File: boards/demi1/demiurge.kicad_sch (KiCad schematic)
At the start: 140 parts, among them J12 Micro_SD_Card_Det_Hirose_DM3AT, J2 Conn_01x06, U1 MCP6002, U10 TL072, U11 TL072, U13 CH32V307RCT6, U2 AMS1117-3.3, U3 MCP6002, U4 AW20036, U5 W25Q128JVS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

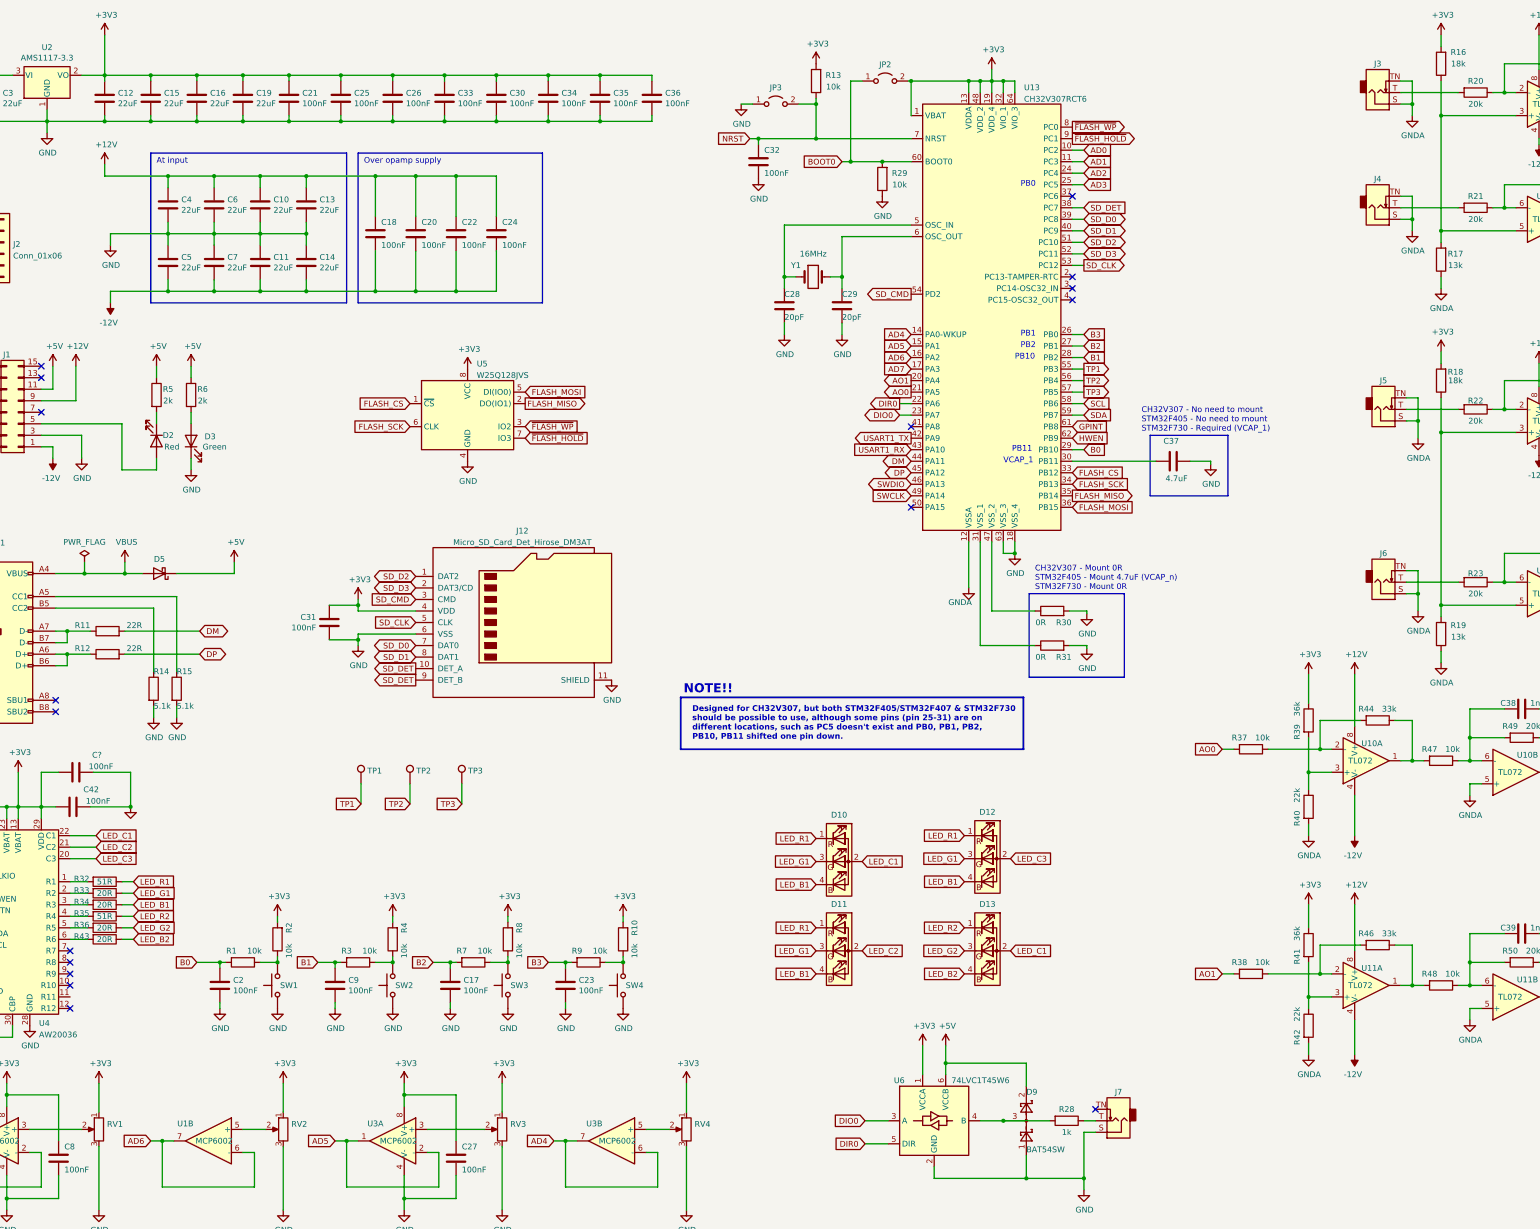
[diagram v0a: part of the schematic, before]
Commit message: Adding testpad for MCO pin, for instance to check clock speeds.
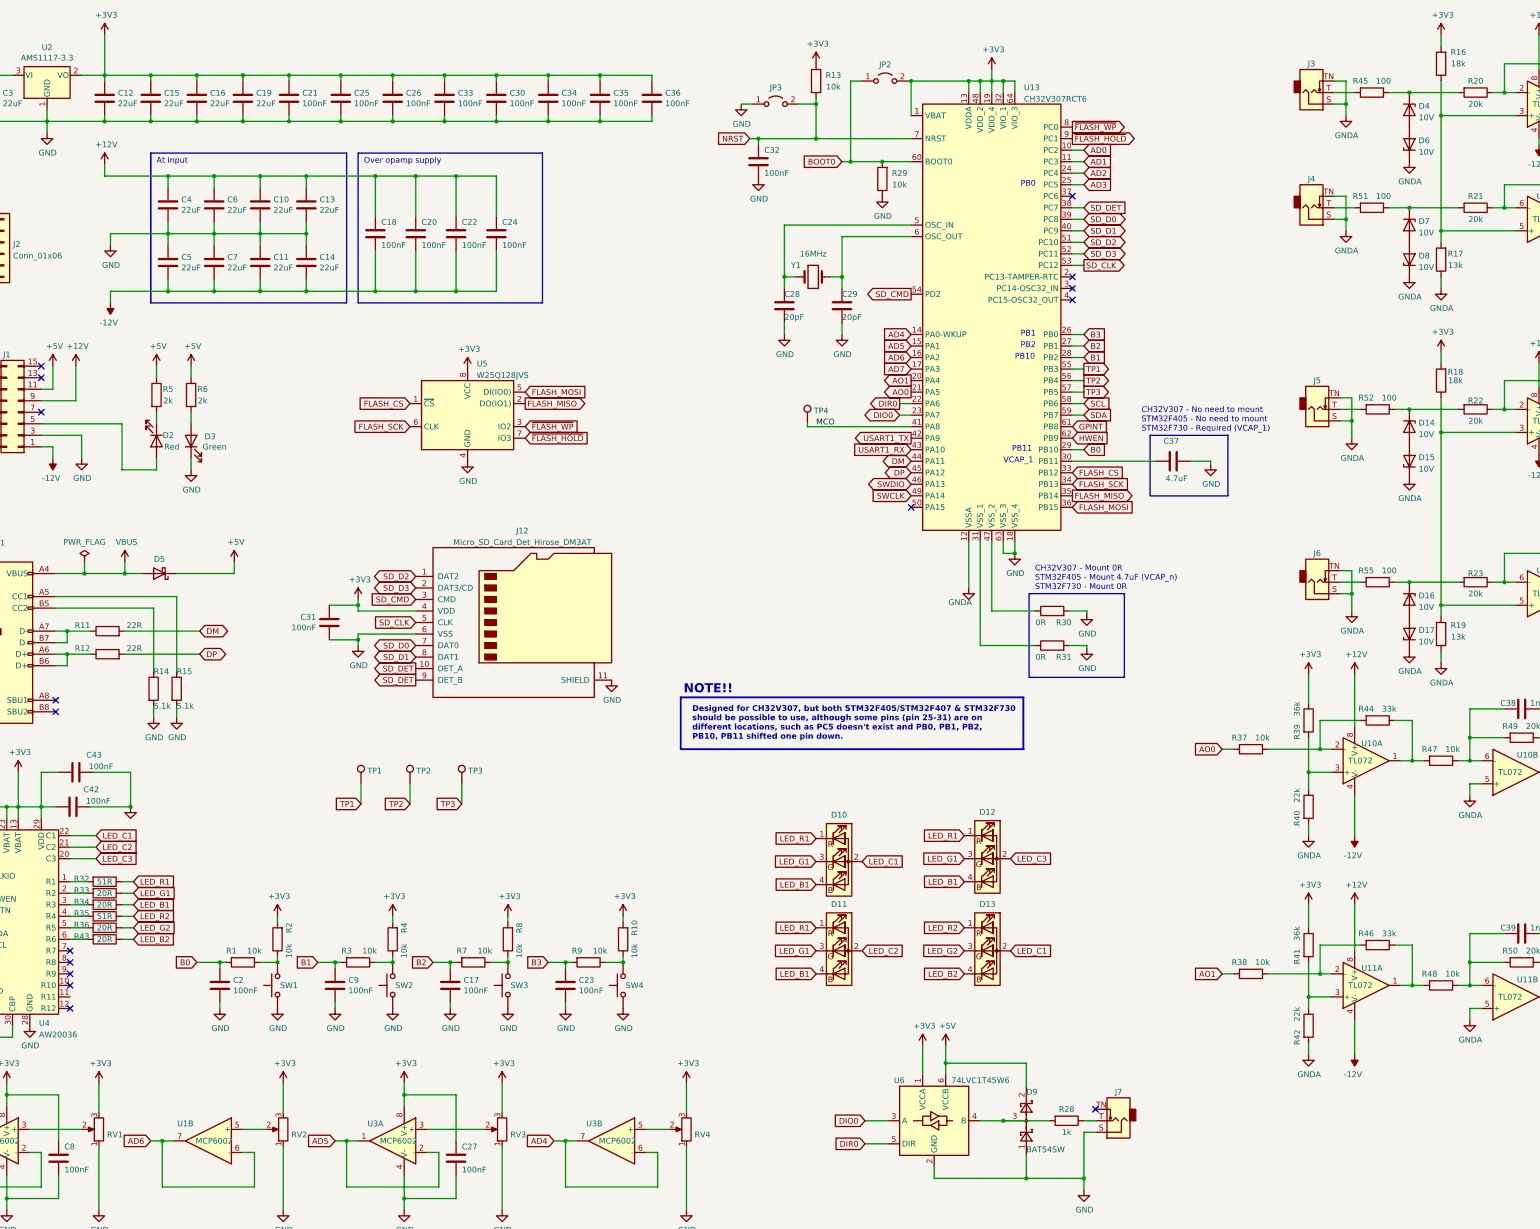
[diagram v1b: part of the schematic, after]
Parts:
- added D14, D15, D16, D17, D4, D6, D7, D8: 10V, Diode_SMD:D_SOD-323, symbol Device:D_Zener
- added R45, R51, R52, R55: 100, Resistor_SMD:R_0603_1608Metric, symbol Device:R
- added TP4: SWO, TestPoint:TestPoint_Pad_1.5x1.5mm, symbol Connector:TestPoint
- JP2, JP3: footprint Jumper:SolderJumper-2_P1.3mm_Open_RoundedPad1.0x1.5mm -> Capacitor_SMD:C_1206_3216Metric
- gave numbers to parts that had none: 1
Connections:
- net +3V3: now also RV1.3, RV2.3, RV3.3, RV4.3; no longer RV1.1, RV2.1, RV3.1, RV4.1
- net GND: now also RV1.1, RV2.1, RV3.1, RV4.1; no longer RV1.3, RV2.3, RV3.3, RV4.3
- net GNDA: now also D15.1 (K), D17.1 (K), D6.1 (K), D8.1 (K)
- net at J4.T: now also R51.2; no longer R21.2
- net at J3.T: now also R45.2; no longer R20.2
- net at J5.T: now also R52.2; no longer R22.2
- net at J6.T: now also R55.2; no longer R23.2
- net MCO: now reaches U13.41 (PA8)
- net MCO: now also TP4.1
- new net: D4.1 (K), R20.2, R45.1
- new net: D7.1 (K), R21.2, R51.1
- new net: D14.1 (K), R22.2, R52.1
- new net: D16.1 (K), R23.2, R55.1
- new net: D7.2 (A), D8.2 (A)
- new net: D14.2 (A), D15.2 (A)
- new net: D4.2 (A), D6.2 (A)
- new net: D16.2 (A), D17.2 (A)
- no-connect marks 23 -> 22
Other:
- moved on the sheet: J3, J4, J5, J6, RV1, RV2, RV3, RV4

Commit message: RevF order made at jlcpcb.
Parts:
- C40: LCSC C14663 -> C15849
- J2: LCSC (none) -> C37208
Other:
- title: Demiurge -> AAA Demiurge 1
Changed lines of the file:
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@@
   (paper "A3")
   (title_block
-    (title "Demiurge")
+    (title "AAA Demiurge 1")
+    (date "2022-08-11")
     (rev "F")
     (company "Awesome Audio Apparatus")
@@
       (effects (font (size 1.27 1.27)) hide)
     )
+    (property "LCSC" "C37208" (id 4) (at 34.925 64.77 0)
+      (effects (font (size 1.27 1.27)) hide)
+    )
     (pin "1")
     (pin "2")
@@
   (symbol (lib_id "Device:C") (at 27.305 240.03 90) (unit 1)
     (in_bom yes) (on_board yes)
-    (property "Reference" "C40" (id 0) (at 31.115 238.76 90)
+    (property "Reference" "C40" (id 0) (at 32.385 238.76 90)
       (effects (font (size 1.27 1.27)) (justify left))
     )
@@
       (effects (font (size 1.27 1.27)) hide)
     )
-    (property "LCSC" "C14663" (id 4) (at 27.305 240.03 0)
+    (property "LCSC" "C15849" (id 4) (at 27.305 240.03 0)
       (effects (font (size 1.27 1.27)) hide)
     )

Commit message: Forgot I2C resistors. Grrr...
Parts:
- added R56, R57: 3k3, Resistor_SMD:R_0603_1608Metric, symbol Device:R
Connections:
- net +3V3: now also R56.2, R57.2
- net SCL: now also R56.1
- net SDA: now also R57.1
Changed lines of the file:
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@@
   (title_block
     (title "AAA Demiurge 1")
-    (date "2022-08-11")
-    (rev "F")
+    (rev "G")
     (company "Awesome Audio Apparatus")
   )
@@
   (junction (at 365.76 139.7) (diameter 0) (color 0 0 0 0)
   )
+  (junction (at 24.765 217.17) (diameter 0) (color 0 0 0 0)
+  )
   (junction (at 330.835 59.69) (diameter 0) (color 0 0 0 0)
   )
@@
   (junction (at 166.37 38.1) (diameter 0) (color 0 0 0 0)
   )
+  (junction (at 19.685 231.14) (diameter 0) (color 0 0 0 0)
+  )
   (junction (at 257.81 133.35) (diameter 0) (color 0 0 0 0)
   )
@@
   (junction (at 113.03 144.78) (diameter 0) (color 0 0 0 0)
   )
+  (junction (at 19.685 219.71) (diameter 0) (color 0 0 0 0)
+  )
   (junction (at 71.12 50.165) (diameter 0) (color 0 0 0 0)
   )
@@
     (stroke (width 0) (type default) (color 0 0 0 0))
   )
+  (wire (pts (xy 17.78 219.71) (xy 19.685 219.71))
+    (stroke (width 0) (type default) (color 0 0 0 0))
+  )
   (wire (pts (xy 250.19 29.21) (xy 250.19 31.75))
     (stroke (width 0) (type default) (color 0 0 0 0))
@@
     (stroke (width 0) (type default) (color 0 0 0 0))
   )
+  (wire (pts (xy 13.97 227.33) (xy 13.97 231.14))
+    (stroke (width 0) (type default) (color 0 0 0 0))
+  )
   (wire (pts (xy 45.72 97.155) (xy 45.72 92.075))
     (stroke (width 0) (type default) (color 0 0 0 0))
@@
     (stroke (width 0) (type default) (color 0 0 0 0))
   )
+  (wire (pts (xy 13.97 231.14) (xy 19.685 231.14))
+    (stroke (width 0) (type default) (color 0 0 0 0))
+  )
   (wire (pts (xy 48.895 150.495) (xy 53.975 150.495))
     (stroke (width 0) (type default) (color 0 0 0 0))
@@
     (stroke (width 0) (type default) (color 0 0 0 0))
   )
+  (wire (pts (xy 17.78 217.17) (xy 24.765 217.17))
+    (stroke (width 0) (type default) (color 0 0 0 0))
+  )
   (wire (pts (xy 273.05 57.15) (xy 270.51 57.15))
     (stroke (width 0) (type default) (color 0 0 0 0))
@@
     (stroke (width 0) (type default) (color 0 0 0 0))
   )
+  (wire (pts (xy 24.765 217.17) (xy 24.765 220.98))
+    (stroke (width 0) (type default) (color 0 0 0 0))
+  )
   (wire (pts (xy 234.95 29.21) (xy 247.65 29.21))
     (stroke (width 0) (type default) (color 0 0 0 0))
@@
     (stroke (width 0) (type default) (color 0 0 0 0))
   )
+  (wire (pts (xy 19.685 220.98) (xy 19.685 219.71))
+    (stroke (width 0) (type default) (color 0 0 0 0))
+  )
   (wire (pts (xy 113.03 152.4) (xy 113.03 153.67))
     (stroke (width 0) (type default) (color 0 0 0 0))
@@
     (stroke (width 0) (type default) (color 0 0 0 0))
   )
+  (wire (pts (xy 19.685 219.71) (xy 29.21 219.71))
+    (stroke (width 0) (type default) (color 0 0 0 0))
+  )
   (wire (pts (xy 270.51 67.31) (xy 273.05 67.31))
     (stroke (width 0) (type default) (color 0 0 0 0))
@@
     (stroke (width 0) (type default) (color 0 0 0 0))
   )
+  (wire (pts (xy 24.765 231.14) (xy 24.765 228.6))
+    (stroke (width 0) (type default) (color 0 0 0 0))
+  )
+  (wire (pts (xy 19.685 231.14) (xy 24.765 231.14))
+    (stroke (width 0) (type default) (color 0 0 0 0))
+  )
   (wire (pts (xy 35.56 191.77) (xy 35.56 189.23))
     (stroke (width 0) (type default) (color 0 0 0 0))
@@
     (stroke (width 0) (type default) (color 0 0 0 0))
   )
+  (wire (pts (xy 19.685 228.6) (xy 19.685 231.14))
+    (stroke (width 0) (type default) (color 0 0 0 0))
+  )
   (wire (pts (xy 351.79 106.68) (xy 351.79 99.06))
     (stroke (width 0) (type default) (color 0 0 0 0))
@@
     (stroke (width 0) (type default) (color 0 0 0 0))
   )
+  (wire (pts (xy 24.765 217.17) (xy 29.21 217.17))
+    (stroke (width 0) (type default) (color 0 0 0 0))
+  )
   (wire (pts (xy 234.95 60.96) (xy 207.01 60.96))
     (stroke (width 0) (type default) (color 0 0 0 0))
@@
     )
   )
-  (global_label "SDA" (shape input) (at 29.21 217.17 180) (fields_autoplaced)
+  (global_label "SDA" (shape input) (at 17.78 217.17 180) (fields_autoplaced)
     (effects (font (size 1.27 1.27)) (justify right))
-    (property "Intersheet References" "${INTERSHEET_REFS}" (id 0) (at 7.62 5.08 0)
+    (property "Intersheet References" "${INTERSHEET_REFS}" (id 0) (at -3.81 5.08 0)
       (effects (font (size 1.27 1.27)) hide)
     )
@@
     )
   )
-  (global_label "SCL" (shape input) (at 29.21 219.71 180) (fields_autoplaced)
+  (global_label "SCL" (shape input) (at 17.78 219.71 180) (fields_autoplaced)
     (effects (font (size 1.27 1.27)) (justify right))
-    (property "Intersheet References" "${INTERSHEET_REFS}" (id 0) (at 7.62 10.16 0)
+    (property "Intersheet References" "${INTERSHEET_REFS}" (id 0) (at -3.81 10.16 0)
       (effects (font (size 1.27 1.27)) hide)
     )
@@
     (pin "1")
   )
+  (symbol (lib_id "power:+3V3") (at 13.97 227.33 0) (unit 1)
+    (in_bom yes) (on_board yes)
+    (property "Reference" "#PWR078" (id 0) (at 13.97 231.14 0)
+      (effects (font (size 1.27 1.27)) hide)
+    )
+    (property "Value" "+3V3" (id 1) (at 14.351 222.9358 0))
+    (property "Footprint" "" (id 2) (at 13.97 227.33 0)
+      (effects (font (size 1.27 1.27)) hide)
+    )
+    (property "Datasheet" "" (id 3) (at 13.97 227.33 0)
+      (effects (font (size 1.27 1.27)) hide)
+    )
+    (pin "1")
+  )
   (symbol (lib_id "power:+3V3") (at 213.995 25.4 0) (unit 1)
     (in_bom yes) (on_board yes)
@@
     (pin "1")
   )
+  (symbol (lib_id "Device:R") (at 19.685 224.79 0) (unit 1)
+    (in_bom yes) (on_board yes)
+    (property "Reference" "R56" (id 0) (at 19.685 227.33 90)
+      (effects (font (size 1.27 1.27)) (justify left))
+    )
+    (property "Value" "3k3" (id 1) (at 22.225 224.79 90))
+    (property "Footprint" "Resistor_SMD:R_0603_1608Metric" (id 2) (at 17.907 224.79 90)
+      (effects (font (size 1.27 1.27)) hide)
+    )
+    (property "Datasheet" "~" (id 3) (at 19.685 224.79 0)
+      (effects (font (size 1.27 1.27)) hide)
+    )
+    (property "LCSC" "C22978" (id 4) (at 19.685 224.79 90)
+      (effects (font (size 1.27 1.27)) hide)
+    )
+    (pin "1")
+    (pin "2")
+  )
   (symbol (lib_id "power:GND") (at 137.16 113.03 0) (unit 1)
     (in_bom yes) (on_board yes)
@@
     (pin "1")
   )
+  (symbol (lib_id "Device:R") (at 24.765 224.79 0) (unit 1)
+    (in_bom yes) (on_board yes)
+    (property "Reference" "R57" (id 0) (at 24.765 227.33 90)
+      (effects (font (size 1.27 1.27)) (justify left))
+    )
+    (property "Value" "3k3" (id 1) (at 27.305 224.79 90))
+    (property "Footprint" "Resistor_SMD:R_0603_1608Metric" (id 2) (at 22.987 224.79 90)
+      (effects (font (size 1.27 1.27)) hide)
+    )
+    (property "Datasheet" "~" (id 3) (at 24.765 224.79 0)
+      (effects (font (size 1.27 1.27)) hide)
+    )
+    (property "LCSC" "C22978" (id 4) (at 24.765 224.79 90)
+      (effects (font (size 1.27 1.27)) hide)
+    )
+    (pin "1")
+    (pin "2")
+  )
   (symbol (lib_id "power:GND") (at 18.415 204.47 0) (unit 1)
     (in_bom yes) (on_board yes)
@@
       (reference "#PWR077") (unit 1) (value "GNDA") (footprint "")
     )
+    (path "/0117f9ef-6db9-4470-98ab-592fcb3cec5a"
+      (reference "#PWR078") (unit 1) (value "+3V3") (footprint "")
+    )
     (path "/00000000-0000-0000-0000-00005feded9f"
       (reference "#PWR0103") (unit 1) (value "+3V3") (footprint "")
@@
       (reference "R55") (unit 1) (value "100") (footprint "Resistor_SMD:R_0603_1608Metric")
     )
+    (path "/6c93caa9-cfe8-4620-aa24-dadbe856362c"
+      (reference "R56") (unit 1) (value "3k3") (footprint "Resistor_SMD:R_0603_1608Metric")
+    )
+    (path "/d94dd0f4-2c79-4924-a210-2928f4485101"
+      (reference "R57") (unit 1) (value "3k3") (footprint "Resistor_SMD:R_0603_1608Metric")
+    )
     (path "/00000000-0000-0000-0000-00005dc42390"

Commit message: Adding comment that STM32F446 can also be used.
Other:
- note added: "CH32V307 - Mount 0R STM32F405 - Mount 4.7uF (VCAP_n) STM32F446 - Mount 0R STM32F730 - Mount 0R"
- note added: "CH32V307 - No need to mount STM32F405 - No need to mount STM32F446 - Required (VCAP_1) STM32F730 - Required (VCAP_1)"
- note added: "Designed for CH32V307, but STM32F405/STM32F407, STM32F446 & STM32F730 should be possible to use, although some pins (pin 25-31) are on different locations, such as PC5 doesn't exist and PB0, PB1, PB2, PB10, PB11 shifted one pin down."
- note removed: "CH32V307 - Mount 0R STM32F405 - Mount 4.7uF (VCAP_n) STM32F730 - Mount 0R"
- note removed: "CH32V307 - No need to mount STM32F405 - No need to mount STM32F730 - Required (VCAP_1)"
- note removed: "Designed for CH32V307, but both STM32F405/STM32F407 & STM32F730 should be possible to use, although some pins (pin 25-31) are on different locations, such as PC5 doesn't exist and PB0, PB1, PB2, PB10, PB11 shifted one pin down."
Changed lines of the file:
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@@
     (stroke (width 0) (type default) (color 0 0 0 0))
   )
-  (text "Designed for CH32V307, but both STM32F405/STM32F407 & STM32F730\nshould be possible to use, although some pins (pin 25-31) are on \ndifferent locations, such as PC5 doesn't exist and PB0, PB1, PB2, \nPB10, PB11 shifted one pin down."
+  (text "Designed for CH32V307, but STM32F405/STM32F407, STM32F446 & \nSTM32F730 should be possible to use, although some pins (pin 25-31)  \nare on different locations, such as PC5 doesn't exist and PB0, PB1,  \nPB2, PB10, PB11 shifted one pin down."
     (at 186.69 174.625 0)
     (effects (font (size 1.27 1.27) (thickness 0.254) bold) (justify left bottom))
@@
     (effects (font (size 1.27 1.27)) (justify left bottom))
   )
-  (text "CH32V307 - No need to mount\nSTM32F405 - No need to mount\nSTM32F730 - Required (VCAP_1)"
+  (text "CH32V307 - No need to mount\nSTM32F405 - No need to mount\nSTM32F446 - Required (VCAP_1)\nSTM32F730 - Required (VCAP_1)"
     (at 285.75 106.68 0)
     (effects (font (size 1.27 1.27)) (justify left bottom))
   )
-  (text "CH32V307 - Mount 0R\nSTM32F405 - Mount 4.7uF (VCAP_n)\nSTM32F730 - Mount 0R"
+  (text "CH32V307 - Mount 0R\nSTM32F405 - Mount 4.7uF (VCAP_n)\nSTM32F446 - Mount 0R\nSTM32F730 - Mount 0R"
     (at 262.255 141.605 0)
     (effects (font (size 1.27 1.27)) (justify left bottom))

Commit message: RevG using STM32F446.
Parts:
- U13: value CH32V307RCT6 -> STM32F446; LCSC CH32V307RCT6 -> C69336
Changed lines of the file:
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@@
   (title_block
     (title "AAA Demiurge 1")
+    (date "2022-10-02")
     (rev "G")
     (company "Awesome Audio Apparatus")
@@
       (effects (font (size 1.27 1.27)) (justify left))
     )
-    (property "Value" "CH32V307RCT6" (id 1) (at 259.8294 33.1779 0)
+    (property "Value" "STM32F446" (id 1) (at 259.8294 33.1779 0)
       (effects (font (size 1.27 1.27)) (justify left))
     )
@@
       (effects (font (size 1.27 1.27)) hide)
     )
-    (property "LCSC" "CH32V307RCT6" (id 4) (at 252.73 81.28 0)
+    (property "LCSC" "C69336" (id 4) (at 252.73 81.28 0)
       (effects (font (size 1.27 1.27)) hide)
     )
@@
     )
     (path "/656368b3-f557-4826-ae34-bd6d81988e01"
-      (reference "U13") (unit 1) (value "CH32V307RCT6") (footprint "Package_QFP:LQFP-64_10x10mm_P0.5mm")
+      (reference "U13") (unit 1) (value "STM32F446") (footprint "Package_QFP:LQFP-64_10x10mm_P0.5mm")
     )
     (path "/00000000-0000-0000-0000-00006068bd74"
